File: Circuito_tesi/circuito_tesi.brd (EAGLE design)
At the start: 100 x 80 mm, 37 parts, among them IC1.8 317T, IC3.3 317T, IC5 317T, Q1 BSS138, U1 NRF52832, U2 SGP30, U3 MICS-6814, U4 OPA2277PA, U6 BME280, U7 LIS3DH

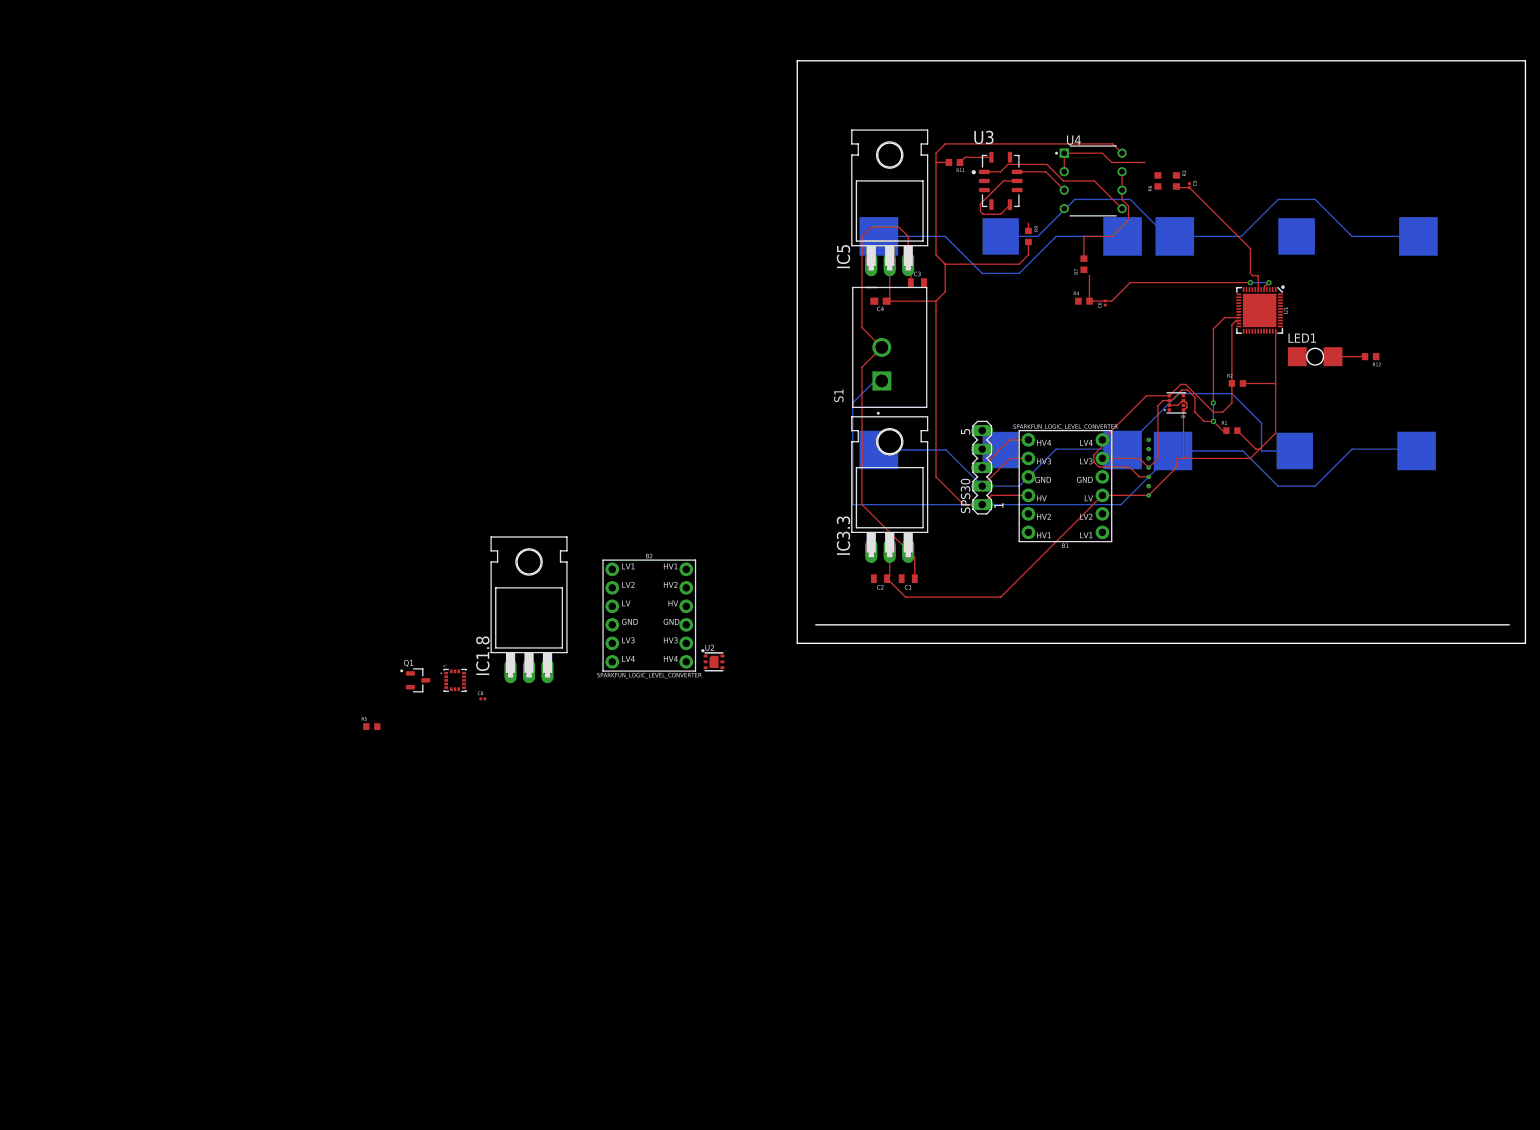
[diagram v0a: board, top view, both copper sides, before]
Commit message: Cambiate resistenze a 1/4 W max
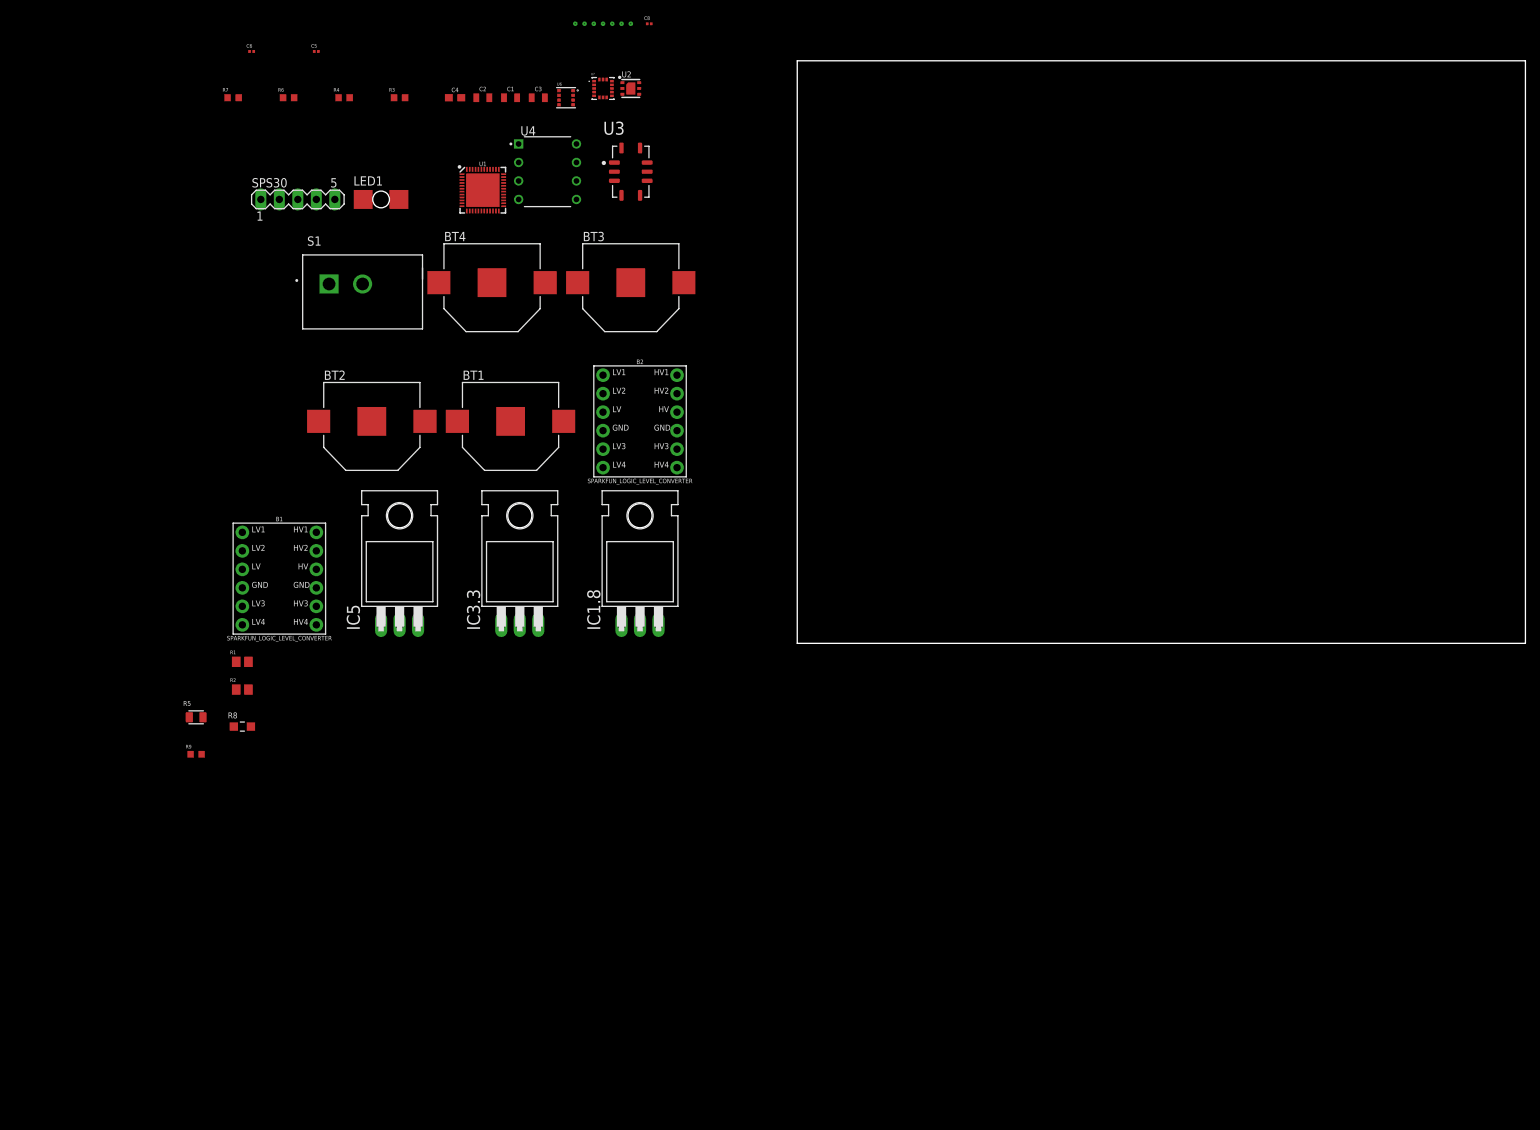
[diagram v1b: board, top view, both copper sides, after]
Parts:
- removed Q1: BSS138, BSS138:SOT95P240X111-3N
- removed R11: RMCF0603FT130R, Res_130OHM:RESC1508X55N
- removed R12: RMCF0603FT300R, Res_300OHM:RESC1508X55N
- added R8: ERA6VEB8200V, Res_820_0p25W:RES_ERA6VEB8200V
- BT1, BT2, BT3, BT4: value BHX1-2450-SM -> 2996TR; device BHX1-2450-SM:BAT_BHX1-2450-SM -> Battery_holder:BAT_2996TR
- R1, R2: value RNCF0603BTE10K0 -> RNCP0805FTD10K0; device Res_10KOHM:RESC1508X55N -> Res_10K_0p25W:RESC2012X60N
- R5: value RNCF0603BTE10K0 -> RP73PF2A130RBTDF; device Res_10KOHM:RESC1508X55N -> Res_130_0p25:RESC2012X65N
- moved R2 143.0 mm to (-76.2, -6.35)
- moved R1 139.5 mm to (-76.2, -2.54)
- moved R9 134.6 mm to (-82.5, -15.2), turned to 0 degrees
- moved LED1 130.1 mm to (-57.1, 61.0)
- moved C6 122.2 mm to (-74.9, 81.3), turned to 0 degrees
- moved C5 121.3 mm to (-66.0, 81.3), turned to 0 degrees
- moved R6 119.9 mm to (-69.8, 74.9), turned to 0 degrees
- moved R7 119.1 mm to (-77.5, 74.9), turned to 0 degrees
- moved BT4 110.7 mm to (-41.9, 49.5), flipped to the top
- moved B1 108.7 mm to (-71.1, 8.89), turned to 0 degrees
- moved U1 108.0 mm to (-43.2, 62.2), turned to 0 degrees
- moved BT1 107.8 mm to (-39.4, 30.5), flipped to the top
- moved R3 107.3 mm to (-54.6, 74.9), turned to 0 degrees
- moved R4 105.4 mm to (-62.2, 74.9)
- moved SPS30 100.9 mm to (-68.6, 61.0), turned to 0 degrees
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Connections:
- removed net N$8: R5.2
- net 5V: now also R5.2, R8.2; no longer R11.2, R9.2
- net GND: now also BT4.-, R9.1; no longer BT4.2, R12.1
- net N$11: now also R8.1; no longer R9.1
- net N$13: now also R5.1; no longer R11.1
- net N$19: now also BT1.S+1, BT1.S+2; no longer BT1.1, BT1.1_1
- net N$2: now also BT1.-, BT2.S+1, BT2.S+2; no longer BT1.2, BT2.1, BT2.1_1
- net N$4: now also BT2.-, BT3.S+1, BT3.S+2; no longer BT2.2, BT3.1, BT3.1_1
- net N$5: now also BT3.-, BT4.S+1, BT4.S+2; no longer BT3.2, BT4.1, BT4.1_1
- net N$9: now also R9.2; no longer R12.2
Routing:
- net 5V: track 114.5 -> 0.00 mm
- net N$19: track 104.0 -> 0.00 mm
- net 3.3: track 101.9 -> 0.00 mm
- net N$2: track 70.0 -> 0.00 mm
- net VDD: track 66.2 -> 0.00 mm
- net N$5: track 64.3 -> 0.00 mm
- net SCL: track 47.0 -> 0.00 mm
- net SDA: track 46.5 -> 0.00 mm, vias 2 -> 0
- net N$4: track 37.7 -> 0.00 mm
- net N$15: track 30.5 -> 0.00 mm, vias 2 -> 0
- net N$6: track 21.9 -> 0.00 mm
- net N$17: track 20.2 -> 0.00 mm
- net N$7: track 17.1 -> 0.00 mm
- net N$22: track 14.1 -> 0.00 mm
- net N$11: track 13.2 -> 0.00 mm
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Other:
- outline, holes or cut-outs redrawn

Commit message: Aggiunte nuovi condensatori e voltage regulator
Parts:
- removed IC1.8, IC3.3, IC5: 317T, linear:TO220H
- added C7: GRM033C80J104KE15D, Condens_100nF:CAPC0603X33N
- added C9: GRM033R60J103KA01D, Condens_10nF:CAPC0603X33N
- added V_REG_1.8: MCP1825S-1802E/DB, V_Reg_1.8_SMD:SOT230P700X180-4N
- added V_REG_3.3: LD1117S33TR, V_Reg_3.3_SMD:SOT230P700X180-4N
- added V_REG_5: LDL1117S50RSOT223_STM-L, V_Reg_5_SMD:SOT223_STM-L
- C1: value 10uF -> GRM033C80J104KE15D; device SparkFun-Capacitors:0805 -> Condens_100nF:CAPC0603X33N
- C2: value 10uF -> CL05A106MP5NUNC; device SparkFun-Capacitors:0805 -> Condens_10uF:CAPC1005X55N
- C3: value 0.33µF -> GRM035R60G475ME15D; device SparkFun-Capacitors:0805 -> Condens_4.7uF:CAPC0603X55N
- C4: value 0.1uF -> GRM033R60J105MEA2D; device SparkFun-Capacitors:0603 -> Condens_1uF:CAPC0603X35N
- C5: value GRM033R60J103KA01D -> GRM033R60J105MEA2D; device Condens_10nF:CAPC0603X33N -> Condens_1uF:CAPC0603X35N
- C6: value GRM033R60J103KA01D -> GRM035R60G475ME15D; device Condens_10nF:CAPC0603X33N -> Condens_4.7uF:CAPC0603X55N
- C8: value GRM033C80J104KE15D -> GRM033R60J103KA01D; device Condens_100nF:CAPC0603X33N -> Condens_10nF:CAPC0603X33N
- R5: value RP73PF2A130RBTDF -> RMCF0603FT5M10; device Res_130_0p25:RESC2012X65N -> Res_5.1MOHM:RESC1508X55N
- R7: value RMCF0603FT5M10 -> RP73PF2A130RBTDF; device Res_5.1MOHM:RESC1508X55N -> Res_130_0p25:RESC2012X65N
- moved C3 139.0 mm to (-106.7, -44.5)
- moved C6 137.1 mm to (-106.7, -52.1)
- moved C5 137.0 mm to (-106.7, -49.5)
- moved C4 135.7 mm to (-106.7, -47.0)
- moved C1 133.0 mm to (-102.9, -41.9)
- moved C2 131.9 mm to (-106.7, -40.6)
- moved R5 86.0 mm to (-69.8, 74.9)
- moved R7 85.2 mm to (-82.5, -10.2)
- moved C8 45.9 mm to (-66.0, 81.3)
- moved R6 7.62 mm to (-77.5, 74.9)
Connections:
- net 1.8V: now also C5.2, C7.1, V_REG_1.8.3; no longer C8.1, IC1.8.2
- net 3.3: now also V_REG_3.3.2, V_REG_3.3.4; no longer IC3.3.2
- net 5V: now also C3.2, C6.2, R7.2, V_REG_1.8.1, V_REG_5.4; no longer C4.1, IC5.2, R5.2
- net GND: now also C1.1, C3.1, C4.1, C7.2, C8.1, C9.1, V_REG_1.8.2, V_REG_1.8.4, V_REG_3.3.1, V_REG_5.1; no longer C1.2, C3.2, C4.2, C8.2, IC1.8.1, IC3.3.1, IC5.1
- net N$13: now also R7.1; no longer R5.1
- net N$15: now also C9.2, R6.1; no longer C6.2, R7.1
- net N$17: now also C8.2, R5.2; no longer C5.2, R6.2
- net N$22: now also R5.1; no longer R6.1
- net N$7: now also R6.2; no longer R7.2
- net VDD: now also C1.2, C4.2, V_REG_3.3.3, V_REG_5.3; no longer C1.1, C3.1, IC1.8.3, IC3.3.3, IC5.3

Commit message: Aggiunto SCD4x al circuito
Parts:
- removed SCD4X: SCD4XSCD4X_SCD4X_SCD4X, SCD41-D-R1:SCD4X_SCD4X
- added IC1: SCD41-D-R2, SCD41-R2_unofficial:SCD41DR2
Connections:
- removed net VSS: SCD4X.20, SCD4X.6
- net 3.3: now also IC1.19, IC1.7; no longer SCD4X.19, SCD4X.7
- net GND: now also IC1.20, IC1.21, IC1.6; no longer SCD4X.21
- net SCL: now also IC1.9; no longer SCD4X.9
- net SDA: now also IC1.10; no longer SCD4X.10
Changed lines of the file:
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@@
 <attribute name="VALUE" x="-67.31" y="40.64" size="1.27" layer="27"/>
 </element>
-<element name="SCD4X" library="SCD41-D-R1" package="SCD4X_SCD4X" value="SCD4XSCD4X_SCD4X_SCD4X" x="-30.48" y="85.09" smashed="yes"/>
 <element name="SPS30" library="con-lstb" library_urn="urn:adsk.eagle:library:162" package="MA05-1" package3d_urn="urn:adsk.eagle:package:8332/1" value="" x="-68.58" y="60.96" smashed="yes">
 <attribute name="MF" value="" x="0" y="0" size="1.778" layer="27" display="off"/>
@@
 <attribute name="VALUE" x="-107.41" y="-52.61" size="0.5" layer="27" align="top-left"/>
 </element>
+<element name="IC1" library="SCD41-R2_unofficial" package="SCD41DR2" value="SCD41-D-R2" x="-101.6" y="-59.69" smashed="yes">
+<attribute name="ARROW_PART_NUMBER" value="SCD41-D-R2" x="-101.6" y="-59.69" size="1.778" layer="27" display="off"/>
+<attribute name="ARROW_PRICE-STOCK" value="https://www.arrow.com/en/products/scd41-d-r2/sensirion-ag?region=nac" x="-101.6" y="-59.69" size="1.778" layer="27" display="off"/>
+<attribute name="DESCRIPTION" value="Air Quality Sensor CO2 Sensor 2.5V/3.3V/5V 20-Pin SMD EP" x="-101.6" y="-59.69" size="1.778" layer="27" display="off"/>
+<attribute name="HEIGHT" value="6.8mm" x="-101.6" y="-59.69" size="1.778" layer="27" display="off"/>
+<attribute name="MANUFACTURER_NAME" value="Sensirion" x="-101.6" y="-59.69" size="1.778" layer="27" display="off"/>
+<attribute name="MANUFACTURER_PART_NUMBER" value="SCD41-D-R2" x="-101.6" y="-59.69" size="1.778" layer="27" display="off"/>
+<attribute name="MOUSER_PART_NUMBER" value="403-SCD41-D-R2" x="-101.6" y="-59.69" size="1.778" layer="27" display="off"/>
+<attribute name="MOUSER_PRICE-STOCK" value="https://www.mouser.co.uk/ProductDetail/Sensirion/SCD41-D-R2?qs=HBWAp0VN4Ri4o7ei4T3s0g%3D%3D" x="-101.6" y="-59.69" size="1.778" layer="27" display="off"/>
+<attribute name="NAME" x="-101.6" y="-59.69" size="1.27" layer="25" align="center"/>
+<attribute name="VALUE" x="-101.6" y="-59.69" size="1.27" layer="27" align="center"/>
+</element>
 </elements>
 <signals>
-<signal name="VSS">
-<contactref element="SCD4X" pad="6"/>
-<contactref element="SCD4X" pad="20"/>
-<wire x1="-30.48" y1="85.09" x2="-29.21" y2="85.09" width="0" layer="19" extent="1-1"/>
-</signal>
 <signal name="3.3">
-<contactref element="SCD4X" pad="7"/>
 <contactref element="B1" pad="LV"/>
 <contactref element="U1" pad="13"/>
 <contactref element="U1" pad="36"/>
 <contactref element="U1" pad="48"/>
-<contactref element="U6" pad="2"/>
-<contactref element="U6" pad="6"/>
-<contactref element="U6" pad="8"/>
 <contactref element="B2" pad="HV"/>
-<contactref element="SCD4X" pad="19"/>
 <contactref element="R1" pad="2"/>
 <contactref element="R2" pad="2"/>
@@
 <contactref element="V_REG_3.3" pad="4"/>
 <contactref element="C2" pad="1"/>
+<contactref element="U6" pad="2"/>
+<contactref element="U6" pad="6"/>
+<contactref element="U6" pad="8"/>
+<contactref element="IC1" pad="19"/>
+<contactref element="IC1" pad="7"/>
+<wire x1="-102.85" y1="-55.69" x2="-102.85" y2="-63.69" width="0" layer="19" extent="1-1"/>
+<wire x1="-107.11" y1="-40.64" x2="-102.85" y2="-55.69" width="0" layer="19" extent="1-1"/>
 <wire x1="-103.23" y1="-10.16" x2="-107.11" y2="-40.64" width="0" layer="19" extent="1-1"/>
 <wire x1="-97.43" y1="-10.16" x2="-103.23" y2="-10.16" width="0" layer="19" extent="1-1"/>
@@
 <wire x1="-32.72" y1="75.905" x2="-32.72" y2="74.605" width="0" layer="19" extent="1-1"/>
 <wire x1="-30.78" y1="75.255" x2="-32.72" y2="74.605" width="0" layer="19" extent="1-1"/>
-<wire x1="-27.94" y1="85.09" x2="-30.78" y2="75.255" width="0" layer="19" extent="1-1"/>
-<wire x1="-22.86" y1="85.09" x2="-27.94" y2="85.09" width="0" layer="19" extent="1-1"/>
 <wire x1="-16.51" y1="31.75" x2="-45.38" y2="59.37" width="0" layer="19" extent="1-1"/>
 </signal>
@@
 <contactref element="U1" pad="21"/>
 <contactref element="B1" pad="LV3"/>
-<contactref element="SCD4X" pad="10"/>
 <contactref element="U6" pad="3"/>
 <contactref element="B2" pad="HV3"/>
 <contactref element="R1" pad="1"/>
+<contactref element="IC1" pad="10"/>
+<wire x1="-77.035" y1="-2.54" x2="-99.1" y2="-63.69" width="0" layer="19" extent="1-1"/>
 <wire x1="-76.2" y1="5.08" x2="-77.035" y2="-2.54" width="0" layer="19" extent="1-1"/>
 <wire x1="-16.51" y1="26.67" x2="-76.2" y2="5.08" width="0" layer="19" extent="1-1"/>
 <wire x1="-42.18" y1="59.37" x2="-16.51" y2="26.67" width="0" layer="19" extent="1-1"/>
 <wire x1="-30.78" y1="74.605" x2="-42.18" y2="59.37" width="0" layer="19" extent="1-1"/>
-<wire x1="-26.67" y1="85.09" x2="-30.78" y2="74.605" width="0" layer="19" extent="1-1"/>
 </signal>
 <signal name="SCL">
 <contactref element="B1" pad="LV4"/>
 <contactref element="U1" pad="22"/>
-<contactref element="SCD4X" pad="9"/>
 <contactref element="U6" pad="4"/>
 <contactref element="B2" pad="HV4"/>
 <contactref element="R2" pad="1"/>
+<contactref element="IC1" pad="9"/>
+<wire x1="-77.035" y1="-6.35" x2="-100.35" y2="-63.69" width="0" layer="19" extent="1-1"/>
 <wire x1="-76.2" y1="2.54" x2="-77.035" y2="-6.35" width="0" layer="19" extent="1-1"/>
 <wire x1="-16.51" y1="24.13" x2="-76.2" y2="2.54" width="0" layer="19" extent="1-1"/>
 <wire x1="-41.78" y1="59.37" x2="-16.51" y2="24.13" width="0" layer="19" extent="1-1"/>
 <wire x1="-30.78" y1="73.955" x2="-41.78" y2="59.37" width="0" layer="19" extent="1-1"/>
-<wire x1="-25.4" y1="85.09" x2="-30.78" y2="73.955" width="0" layer="19" extent="1-1"/>
 </signal>
 <signal name="N$6">
@@
 </signal>
 <signal name="GND">
-<contactref element="SCD4X" pad="21"/>
 <contactref element="SPS30" pad="5"/>
 <contactref element="SPS30" pad="4"/>
@@
 <contactref element="C5" pad="1"/>
 <contactref element="C6" pad="1"/>
+<contactref element="IC1" pad="20"/>
+<contactref element="IC1" pad="21"/>
+<contactref element="IC1" pad="6"/>
+<wire x1="-101.6" y1="-59.69" x2="-104.1" y2="-63.69" width="0" layer="19" extent="1-1"/>
+<wire x1="-104.1" y1="-55.69" x2="-101.6" y2="-59.69" width="0" layer="19" extent="1-1"/>
+<wire x1="-106.958" y1="-52.07" x2="-104.1" y2="-55.69" width="0" layer="19" extent="1-1"/>
 <wire x1="-106.96" y1="-49.53" x2="-106.958" y2="-52.07" width="0" layer="19" extent="1-1"/>
 <wire x1="-106.96" y1="-46.99" x2="-106.96" y2="-49.53" width="0" layer="19" extent="1-1"/>
@@
 <wire x1="-32.72" y1="75.255" x2="-30.78" y2="75.905" width="0" layer="19" extent="1-1"/>
 <wire x1="-32.72" y1="73.955" x2="-32.72" y2="75.255" width="0" layer="19" extent="1-1"/>
-<wire x1="-24.13" y1="85.09" x2="-25.445" y2="76.7" width="0" layer="19" extent="1-1"/>
-<wire x1="-20.039" y1="85.09" x2="-24.13" y2="85.09" width="0" layer="19" extent="1-1"/>
+<wire x1="-20.039" y1="85.09" x2="-22.86" y2="76.2" width="0" layer="19" extent="1-1"/>
 <wire x1="-55.37" y1="74.93" x2="-38.26" y2="60.96" width="0" layer="19" extent="1-1"/>
 <wire x1="-62.99" y1="74.93" x2="-55.37" y2="74.93" width="0" layer="19" extent="1-1"/>
